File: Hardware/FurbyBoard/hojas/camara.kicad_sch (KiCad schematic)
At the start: 13 parts, among them J6 FPC 24P 0.5, U8 ME6211C28M5G-N, U9 ME6211C12M5G-N

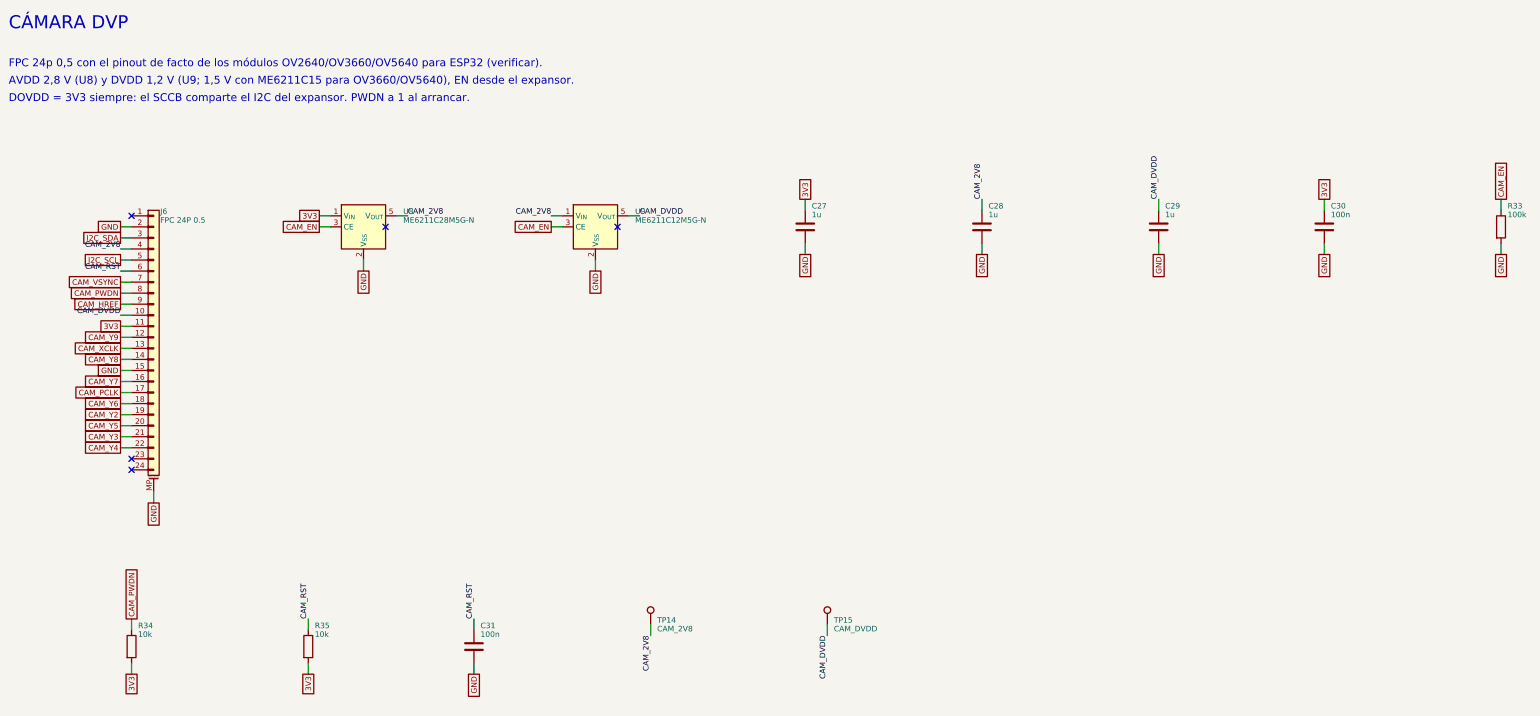
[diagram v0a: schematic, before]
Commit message: Refactor: pads de cable agrupados por zona y etiquetas globales
- Motor en J9 con leva, encoder y sensores; altavoz en J8 con inclinación y
  lengua; luz en J7 con el IR. Desaparecen J4 y J10: cada grupo sale por el
  borde más cercano a su destino.
- Micro en 2x03 en vez de 1x06 para que quepa junto al borde derecho.
- Todas las etiquetas del esquemático son globales, así el nombre de red
  coincide con el del PCB (paridad sin prefijos de hoja).
- ERC 0 errores, 0 avisos.

Co-Authored-By: Claude Opus 5.5 (1M context) <noreply@anthropic.com>
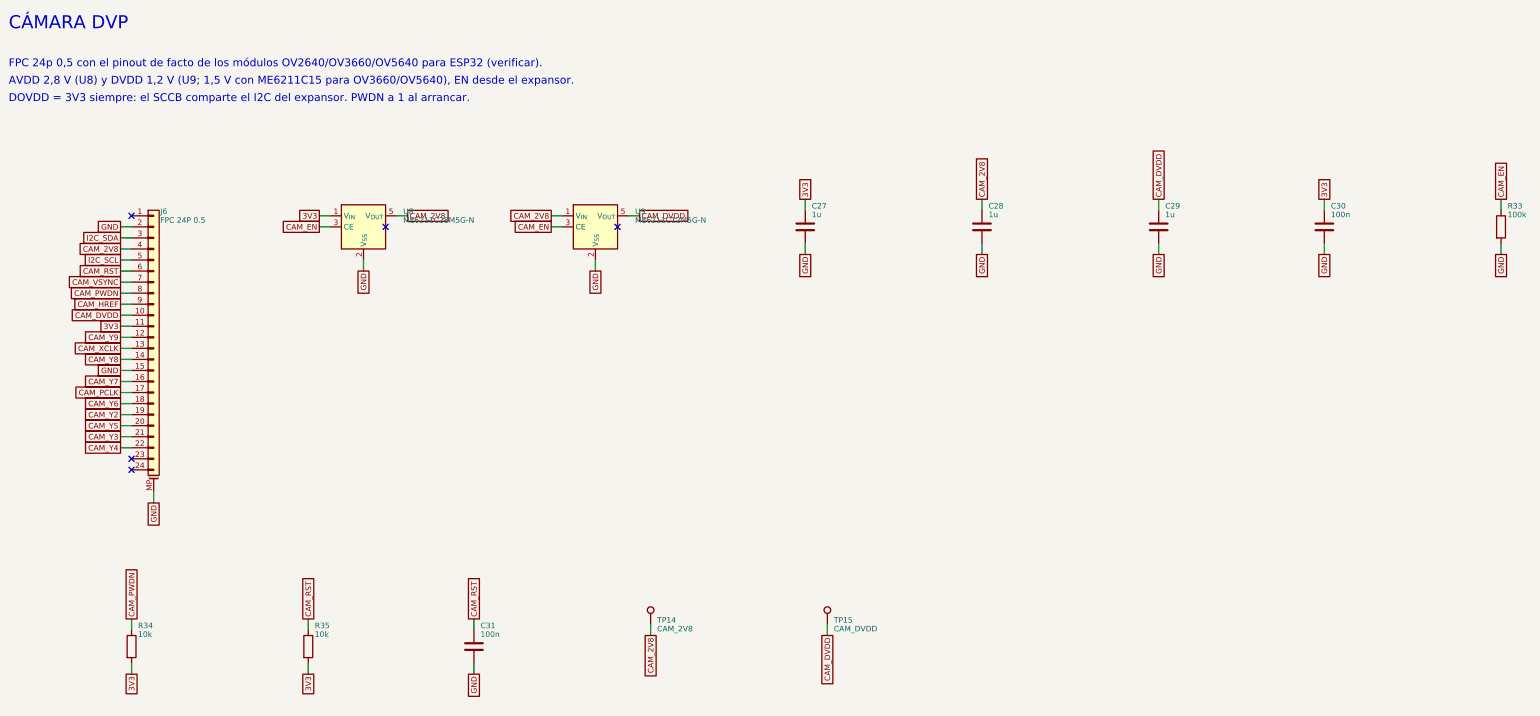
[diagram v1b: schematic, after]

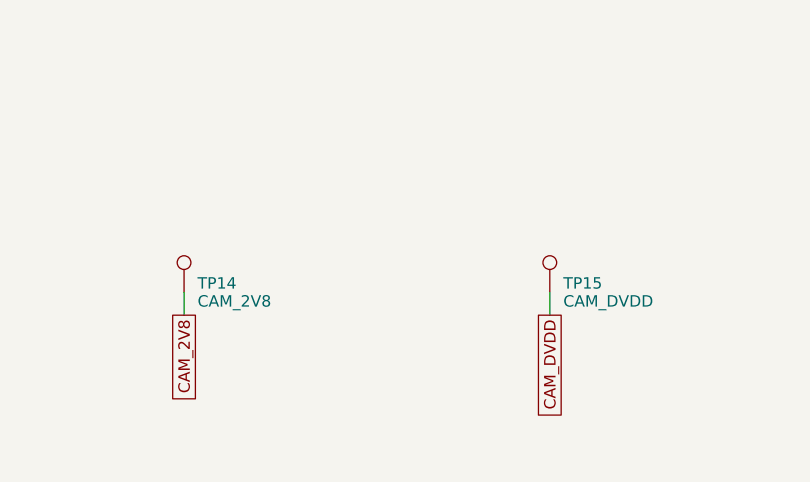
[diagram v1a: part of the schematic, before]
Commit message: Feature: par USB trazado, planos GND/VSYS y serigrafía de la FurbyBoard
- Par USB de J1 al ESD y al módulo, acoplado 0,28/0,15 por F.Cu sobre el
  plano de GND, sin vías (rutas_fijas.py, bloqueado para el autorrutado).
  Canal libre en x -83 bajo la batería.
- In1 plano de GND e In2 plano de VSYS; potencia por pista a 0,4 (cabe en
  los pads de 0,5 de paso) y 3V3 a 0,3. exportar_dsn.py deja el DSN para
  Freerouting con las clases de red.
- Rótulos de serigrafía colocados solos (serigrafia.py): TP, LED, botones,
  puentes y polaridad de la batería arriba; función de cada pad de cable y
  GPIO del J_EXP abajo, con leyenda para J7, J9 y J5.
- Para que quepan los rótulos: fila de LED con resistencias debajo, botones
  en vertical, rejilla de TP con el rótulo debajo. Quedan 14 TP: fuera EN e
  IO0 (se miden en los pads de SW1 y SW2), CHG y PG (en D1 y D2) y un GND.

ERC 0/0. DRC 0 salvo una vía de GND sin plano relleno; sin rutar.

Co-Authored-By: Claude Opus 5.5 (1M context) <noreply@anthropic.com>
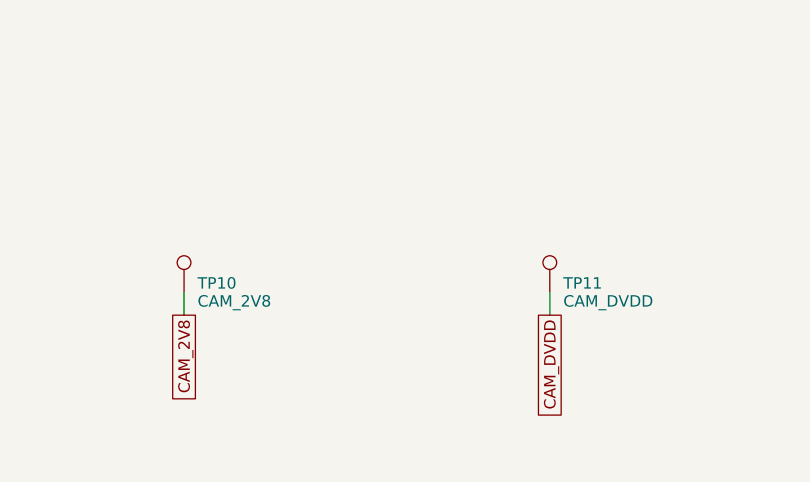
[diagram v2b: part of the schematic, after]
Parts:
- removed TP14: CAM_2V8, TestPoint:TestPoint_Pad_D1.5mm, symbol Connector:TestPoint
- removed TP15: CAM_DVDD, TestPoint:TestPoint_Pad_D1.5mm, symbol Connector:TestPoint
- added TP10: CAM_2V8, TestPoint:TestPoint_Pad_D1.5mm, symbol Connector:TestPoint
- added TP11: CAM_DVDD, TestPoint:TestPoint_Pad_D1.5mm, symbol Connector:TestPoint
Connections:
- net CAM_2V8: now also TP10.1
- net CAM_DVDD: now also TP11.1
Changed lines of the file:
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@@
-	)
-	(symbol
-		(lib_id "Connector:TestPoint")
-		(at 167.64 160.02 0)
-		(unit 1)
-		(body_style 1)
-		(exclude_from_sim no)
-		(in_bom no)
-		(on_board yes)
-		(in_pos_files yes)
-		(dnp no)
-		(property "Reference" "TP14"
-			(at 169.14 159.02 0)
-			(show_name no)
-			(do_not_autoplace no)
-			(effects
-				(font
-					(size 1.27 1.27)
-				)
-				(justify left)
-			)
-		)
-		(property "Value" "CAM_2V8"
-			(at 169.14 161.02 0)
-			(show_name no)
-			(do_not_autoplace no)
-			(effects
-				(font
-					(size 1.27 1.27)
-				)
-				(justify left)
-			)
-		)
-		(property "Footprint" "TestPoint:TestPoint_Pad_D1.5mm"
-			(at 167.64 160.02 0)
-			(hide yes)
-			(show_name no)
-			(do_not_autoplace no)
-			(effects
-				(font
-					(size 1.27 1.27)
-				)
-				(justify left)
-			)
-		)
-		(property "Datasheet" ""
-			(at 167.64 160.02 0)
-			(hide yes)
-			(show_name no)
-			(do_not_autoplace no)
-			(effects
-				(font
-					(size 1.27 1.27)
-				)
-				(justify left)
-			)
-		)
-		(property "Description" "2,80 V con la cámara encendida"
-			(at 167.64 160.02 0)
-			(hide yes)
-			(show_name no)
-			(do_not_autoplace no)
-			(effects
-				(font
-					(size 1.27 1.27)
-				)
-				(justify left)
-			)
-		)
-		(property "LCSC" ""
-			(at 167.64 160.02 0)
-			(hide yes)
-			(show_name no)
-			(do_not_autoplace no)
-			(effects
-				(font
-					(size 1.27 1.27)
-				)
-				(justify left)
-			)
-		)
-		(property "JLC_Class" ""
-			(at 167.64 160.02 0)
-			(hide yes)
-			(show_name no)
-			(do_not_autoplace no)
-			(effects
-				(font
-					(size 1.27 1.27)
-				)
-				(justify left)
-			)
-		)
-		(property "MPN" ""
-			(at 167.64 160.02 0)
-			(hide yes)
-			(show_name no)
-			(do_not_autoplace no)
-			(effects
-				(font
-					(size 1.27 1.27)
-				)
-				(justify left)
-			)
-		)
-		(pin "1"
-		)
-		(instances
-			(project "FurbyBoard"
-				(path "/8b4f1e2a-3c5d-4e6f-9a1b-2c3d4e5f6a7b/560a552f-efe0-507d-88d8-d46e694413a9"
-					(reference "TP14")
-					(unit 1)
-				)
-			)
-		)
 	)
 	(symbol
@@
 	)
 	(symbol
+		(lib_id "Connector:TestPoint")
+		(at 208.28 160.02 0)
+		(unit 1)
+		(body_style 1)
+		(exclude_from_sim no)
+		(in_bom no)
+		(on_board yes)
+		(in_pos_files yes)
+		(dnp no)
+		(property "Reference" "TP11"
+			(at 209.78 159.02 0)
+			(show_name no)
+			(do_not_autoplace no)
+			(effects
+				(font
+					(size 1.27 1.27)
+				)
+				(justify left)
+			)
+		)
+		(property "Value" "CAM_DVDD"
+			(at 209.78 161.02 0)
+			(show_name no)
+			(do_not_autoplace no)
+			(effects
+				(font
+					(size 1.27 1.27)
+				)
+				(justify left)
+			)
+		)
+		(property "Footprint" "TestPoint:TestPoint_Pad_D1.5mm"
+			(at 208.28 160.02 0)
+			(hide yes)
+			(show_name no)
+			(do_not_autoplace no)
+			(effects
+				(font
+					(size 1.27 1.27)
+				)
+				(justify left)
+			)
+		)
+		(property "Datasheet" ""
+			(at 208.28 160.02 0)
+			(hide yes)
+			(show_name no)
+			(do_not_autoplace no)
+			(effects
+				(font
+					(size 1.27 1.27)
+				)
+				(justify left)
+			)
+		)
+		(property "Description" "1,20 V (o 1,50 V) con la cámara encendida"
+			(at 208.28 160.02 0)
+			(hide yes)
+			(show_name no)
+			(do_not_autoplace no)
+			(effects
+				(font
+					(size 1.27 1.27)
+				)
+				(justify left)
+			)
+		)
+		(property "LCSC" ""
+			(at 208.28 160.02 0)
+			(hide yes)
+			(show_name no)
+			(do_not_autoplace no)
+			(effects
+				(font
+					(size 1.27 1.27)
+				)
+				(justify left)
+			)
+		)
+		(property "JLC_Class" ""
+			(at 208.28 160.02 0)
+			(hide yes)
+			(show_name no)
+			(do_not_autoplace no)
+			(effects
+				(font
+					(size 1.27 1.27)
+				)
+				(justify left)
+			)
+		)
+		(property "MPN" ""
+			(at 208.28 160.02 0)
+			(hide yes)
+			(show_name no)
+			(do_not_autoplace no)
+			(effects
+				(font
+					(size 1.27 1.27)
+				)
+				(justify left)
+			)
+		)
+		(pin "1"
+		)
+		(instances
+			(project "FurbyBoard"
+				(path "/8b4f1e2a-3c5d-4e6f-9a1b-2c3d4e5f6a7b/560a552f-efe0-507d-88d8-d46e694413a9"
+					(reference "TP11")
+					(unit 1)
+				)
+			)
+		)
+	)
+	(symbol
+		(lib_id "Connector:TestPoint")
+		(at 167.64 160.02 0)
+		(unit 1)
+		(body_style 1)
+		(exclude_from_sim no)
+		(in_bom no)
+		(on_board yes)
+		(in_pos_files yes)
+		(dnp no)
+		(property "Reference" "TP10"
+			(at 169.14 159.02 0)
+			(show_name no)
+			(do_not_autoplace no)
+			(effects
+				(font
+					(size 1.27 1.27)
+				)
+				(justify left)
+			)
+		)
+		(property "Value" "CAM_2V8"
+			(at 169.14 161.02 0)
+			(show_name no)
+			(do_not_autoplace no)
+			(effects
+				(font
+					(size 1.27 1.27)
+				)
+				(justify left)
+			)
+		)
+		(property "Footprint" "TestPoint:TestPoint_Pad_D1.5mm"
+			(at 167.64 160.02 0)
+			(hide yes)
+			(show_name no)
+			(do_not_autoplace no)
+			(effects
+				(font
+					(size 1.27 1.27)
+				)
+				(justify left)
+			)
+		)
+		(property "Datasheet" ""
+			(at 167.64 160.02 0)
+			(hide yes)
+			(show_name no)
+			(do_not_autoplace no)
+			(effects
+				(font
+					(size 1.27 1.27)
+				)
+				(justify left)
+			)
+		)
+		(property "Description" "2,80 V con la cámara encendida"
+			(at 167.64 160.02 0)
+			(hide yes)
+			(show_name no)
+			(do_not_autoplace no)
+			(effects
+				(font
+					(size 1.27 1.27)
+				)
+				(justify left)
+			)
+		)
+		(property "LCSC" ""
+			(at 167.64 160.02 0)
+			(hide yes)
+			(show_name no)
+			(do_not_autoplace no)
+			(effects
+				(font
+					(size 1.27 1.27)
+				)
+				(justify left)
+			)
+		)
+		(property "JLC_Class" ""
+			(at 167.64 160.02 0)
+			(hide yes)
+			(show_name no)
+			(do_not_autoplace no)
+			(effects
+				(font
+					(size 1.27 1.27)
+				)
+				(justify left)
+			)
+		)
+		(property "MPN" ""
+			(at 167.64 160.02 0)
+			(hide yes)
+			(show_name no)
+			(do_not_autoplace no)
+			(effects
+				(font
+					(size 1.27 1.27)
+				)
+				(justify left)
+			)
+		)
+		(pin "1"
+		)
+		(instances
+			(project "FurbyBoard"
+				(path "/8b4f1e2a-3c5d-4e6f-9a1b-2c3d4e5f6a7b/560a552f-efe0-507d-88d8-d46e694413a9"
+					(reference "TP10")
+					(unit 1)
+				)
+			)
+		)
+	)
+	(symbol
 		(lib_id "Device:R")
 		(at 88.9 165.1 0)
@@
 					(unit 1)
 				)
-			)
-		)
-	)
-	(symbol
-		(lib_id "Connector:TestPoint")
-		(at 208.28 160.02 0)
-		(unit 1)
-		(body_style 1)
-		(exclude_from_sim no)
-		(in_bom no)
-		(on_board yes)
-		(in_pos_files yes)
-		(dnp no)
-		(property "Reference" "TP15"
-			(at 209.78 159.02 0)
-			(show_name no)
-			(do_not_autoplace no)
-			(effects
-				(font
-					(size 1.27 1.27)
-				)
-				(justify left)
-			)
-		)
-		(property "Value" "CAM_DVDD"
-			(at 209.78 161.02 0)
-			(show_name no)
-			(do_not_autoplace no)
-			(effects
-				(font
-					(size 1.27 1.27)
-				)
-				(justify left)
-			)
-		)
-		(property "Footprint" "TestPoint:TestPoint_Pad_D1.5mm"
-			(at 208.28 160.02 0)
-			(hide yes)
-			(show_name no)
-			(do_not_autoplace no)
-			(effects
-				(font
-					(size 1.27 1.27)
-				)
-				(justify left)
-			)
-		)
-		(property "Datasheet" ""
-			(at 208.28 160.02 0)
-			(hide yes)
-			(show_name no)
-			(do_not_autoplace no)
-			(effects
-				(font
-					(size 1.27 1.27)
-				)
-				(justify left)
-			)
-		)
-		(property "Description" "1,20 V (o 1,50 V) con la cámara encendida"
-			(at 208.28 160.02 0)
-			(hide yes)
-			(show_name no)
-			(do_not_autoplace no)
-			(effects
-				(font
-					(size 1.27 1.27)
-				)
-				(justify left)
-			)
-		)
-		(property "LCSC" ""
-			(at 208.28 160.02 0)
-			(hide yes)
-			(show_name no)
-			(do_not_autoplace no)
-			(effects
-				(font
-					(size 1.27 1.27)
-				)
-				(justify left)
-			)
-		)
-		(property "JLC_Class" ""
-			(at 208.28 160.02 0)
-			(hide yes)
-			(show_name no)
-			(do_not_autoplace no)
-			(effects
-				(font
-					(size 1.27 1.27)
-				)
-				(justify left)
-			)
-		)
-		(property "MPN" ""
-			(at 208.28 160.02 0)
-			(hide yes)
-			(show_name no)
-			(do_not_autoplace no)
-			(effects
-				(font
-					(size 1.27 1.27)
-				)
-				(justify left)
-			)
-		)
-		(pin "1"
-		)
-		(instances
-			(project "FurbyBoard"
-				(path "/8b4f1e2a-3c5d-4e6f-9a1b-2c3d4e5f6a7b/560a552f-efe0-507d-88d8-d46e694413a9"
-					(reference "TP15")
-					(unit 1)
-				)

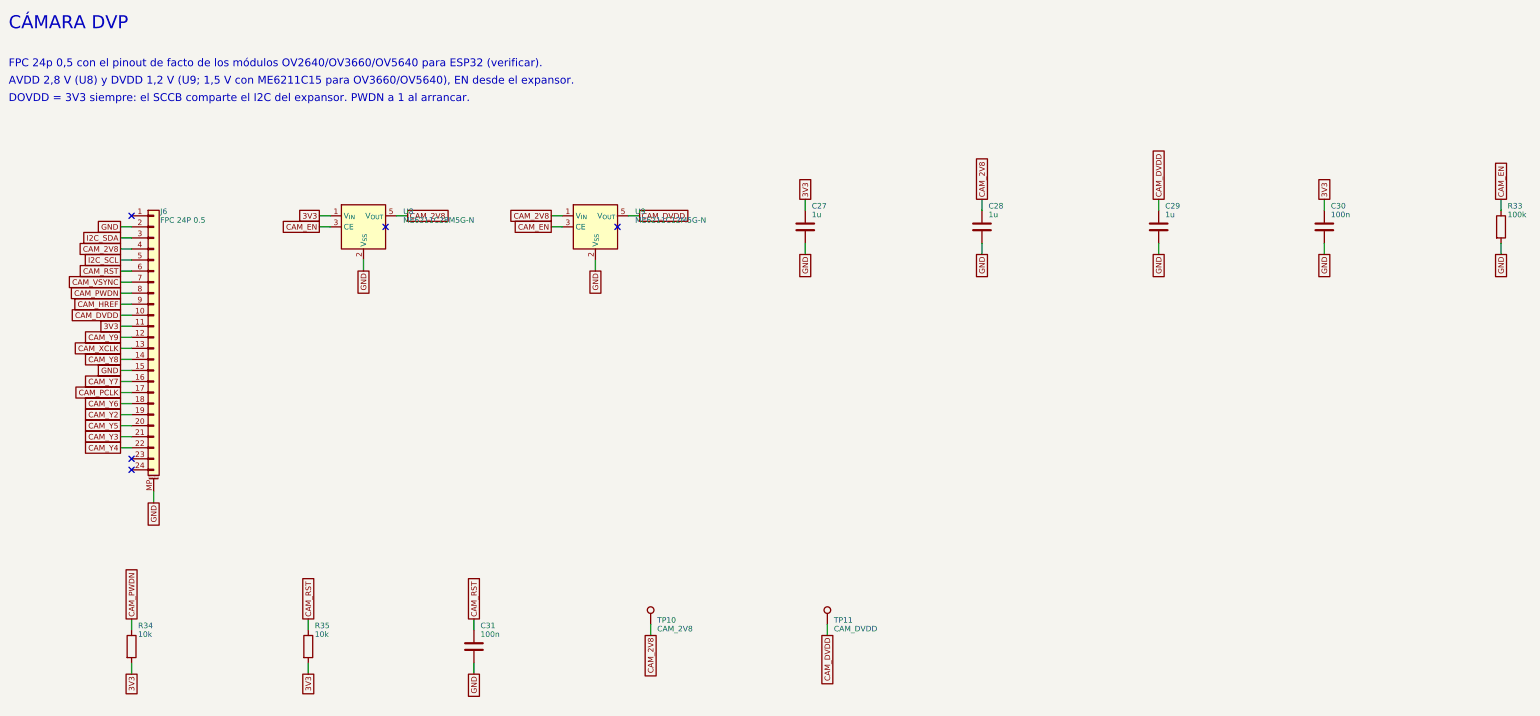
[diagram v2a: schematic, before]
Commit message: Feature: series de 33 Ω en los relojes del bus DVP (M7): R59 en XCLK junto al pin 21 y R60 en PCLK junto a J6
- design.py: R59 y R60, 0402 UNI-ROYAL 33 Ω (C25105, básica); redes nuevas CAM_XCLK_IO
  (pin 21 → R59) y CAM_PCLK_CAM (J6.17 → R60). Rs + Rout ≈ Z0 (≈ 75 Ω de la pista de
  0,15 sobre In1); HREF, VSYNC y los datos no la llevan (motivo en design.py y NOTAS).
- layout.py: R59 en (−72,365; −82,35) bajo el pin 21, entre el patio del módulo y la fila
  del bus; R60 en (−53,6; −78,0) a 2 mm del pad 17 de J6.
- rutas_fijas.py: XCLK acortado por el este hasta R59.2 y entrada al pin 21 desde R59.1
  con una diagonal; PCLK baja a y −78,0 en el tramo de R60 y Y7 a −78,6 (quiebros a 45°
  escalonados). Todo en F.Cu sobre In1, sin vías nuevas.
- pcb-toolkit.toml: CAM_XCLK*/CAM_PCLK* en criticas y en el grupo DVP.

Puertas: ERC 0; DRC con paridad 0/0/0; revisar-rutado 0 errores, 152 avisos (los mismos
por tipo que antes); comprobar-flujo sin errores nuevos (los dos aceptados: I2S_DIN/clase D y
MOT_VREF/L2); rellenos: GND F 2083,0 mm² en 21 trozos (−1,6 mm² por los dos 0402), el resto
igual. PNG revisados en F.Cu a 80 px/mm: comb de J6 con R60 (PCLK y Y7 con sus quiebros,
Y6 y Y8 sin tocar) y fila sur del módulo con R59 (entrada al pin 21, Y8 y Y9 a 0,415).
Paralelos In2/In3: 28 pares, sin cambio (M1 va aparte).

Co-Authored-By: Claude Fable 5.1 <noreply@anthropic.com>
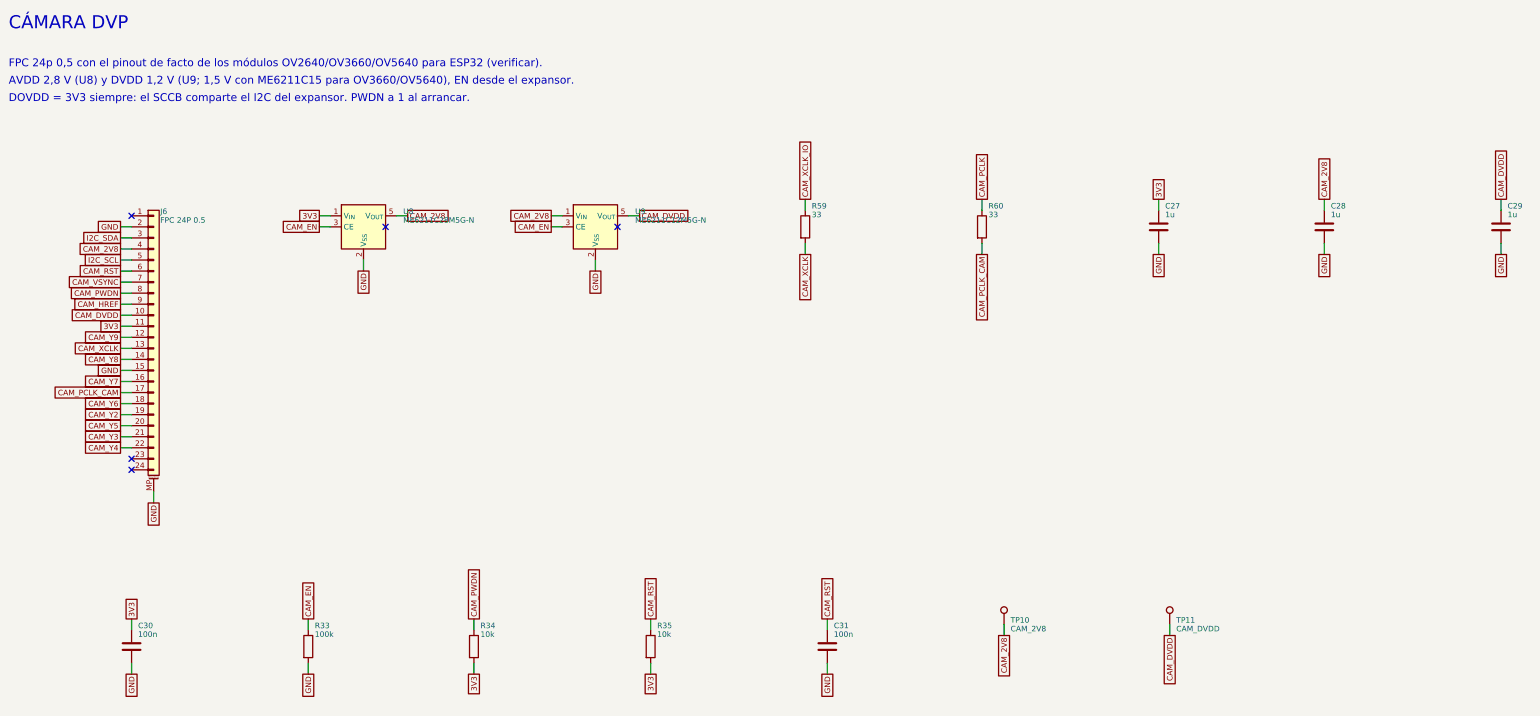
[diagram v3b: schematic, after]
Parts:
- added R59, R60: 33, Resistor_SMD:R_0402_1005Metric, symbol Device:R
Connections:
- net CAM_PCLK: now also R60.1; no longer J6.17 (Pin_17)
- net CAM_XCLK: now also R59.2
- new net CAM_PCLK_CAM: J6.17 (Pin_17), R60.2
- new net CAM_XCLK_IO: R59.1
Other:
- moved on the sheet: C27, C28, C29, C30, C31, R33, R34, R35, TP10, TP11
